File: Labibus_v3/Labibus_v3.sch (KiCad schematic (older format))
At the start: 43 parts, among them J1 Screw_Terminal_01x04, J2 Conn_01x16, J3 Conn_01x06, J4 Conn_01x03, J5 Conn_01x15, J6 Conn_01x12, J7 Conn_01x04 Qwiic JST SH 4-pin, SW1 SW_Push, U1 MIC5205-5.0YM5, U2 MAX485E, U3 ATmega328P-AU, U4 MIC5219-3.3YM5, Y1 Crystal_GND2_Small

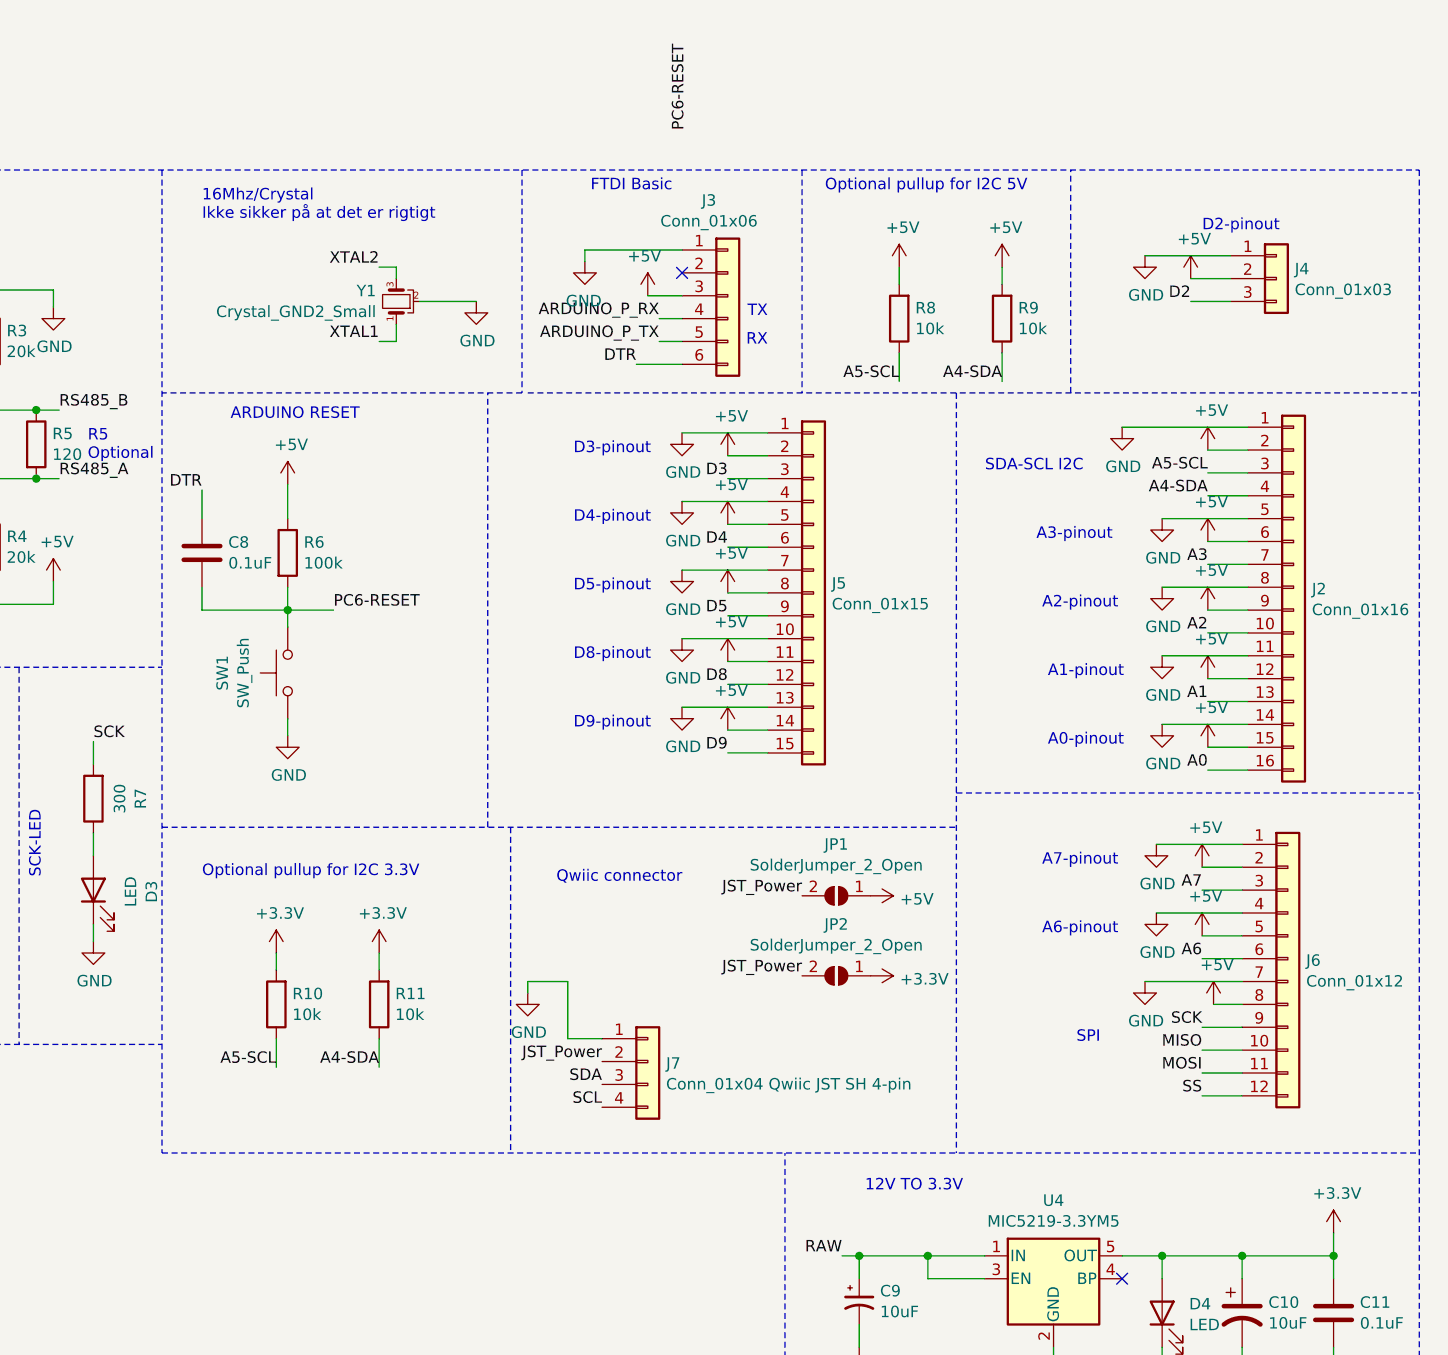
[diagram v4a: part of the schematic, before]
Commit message: update with: 3.3V and 5V select JST connector
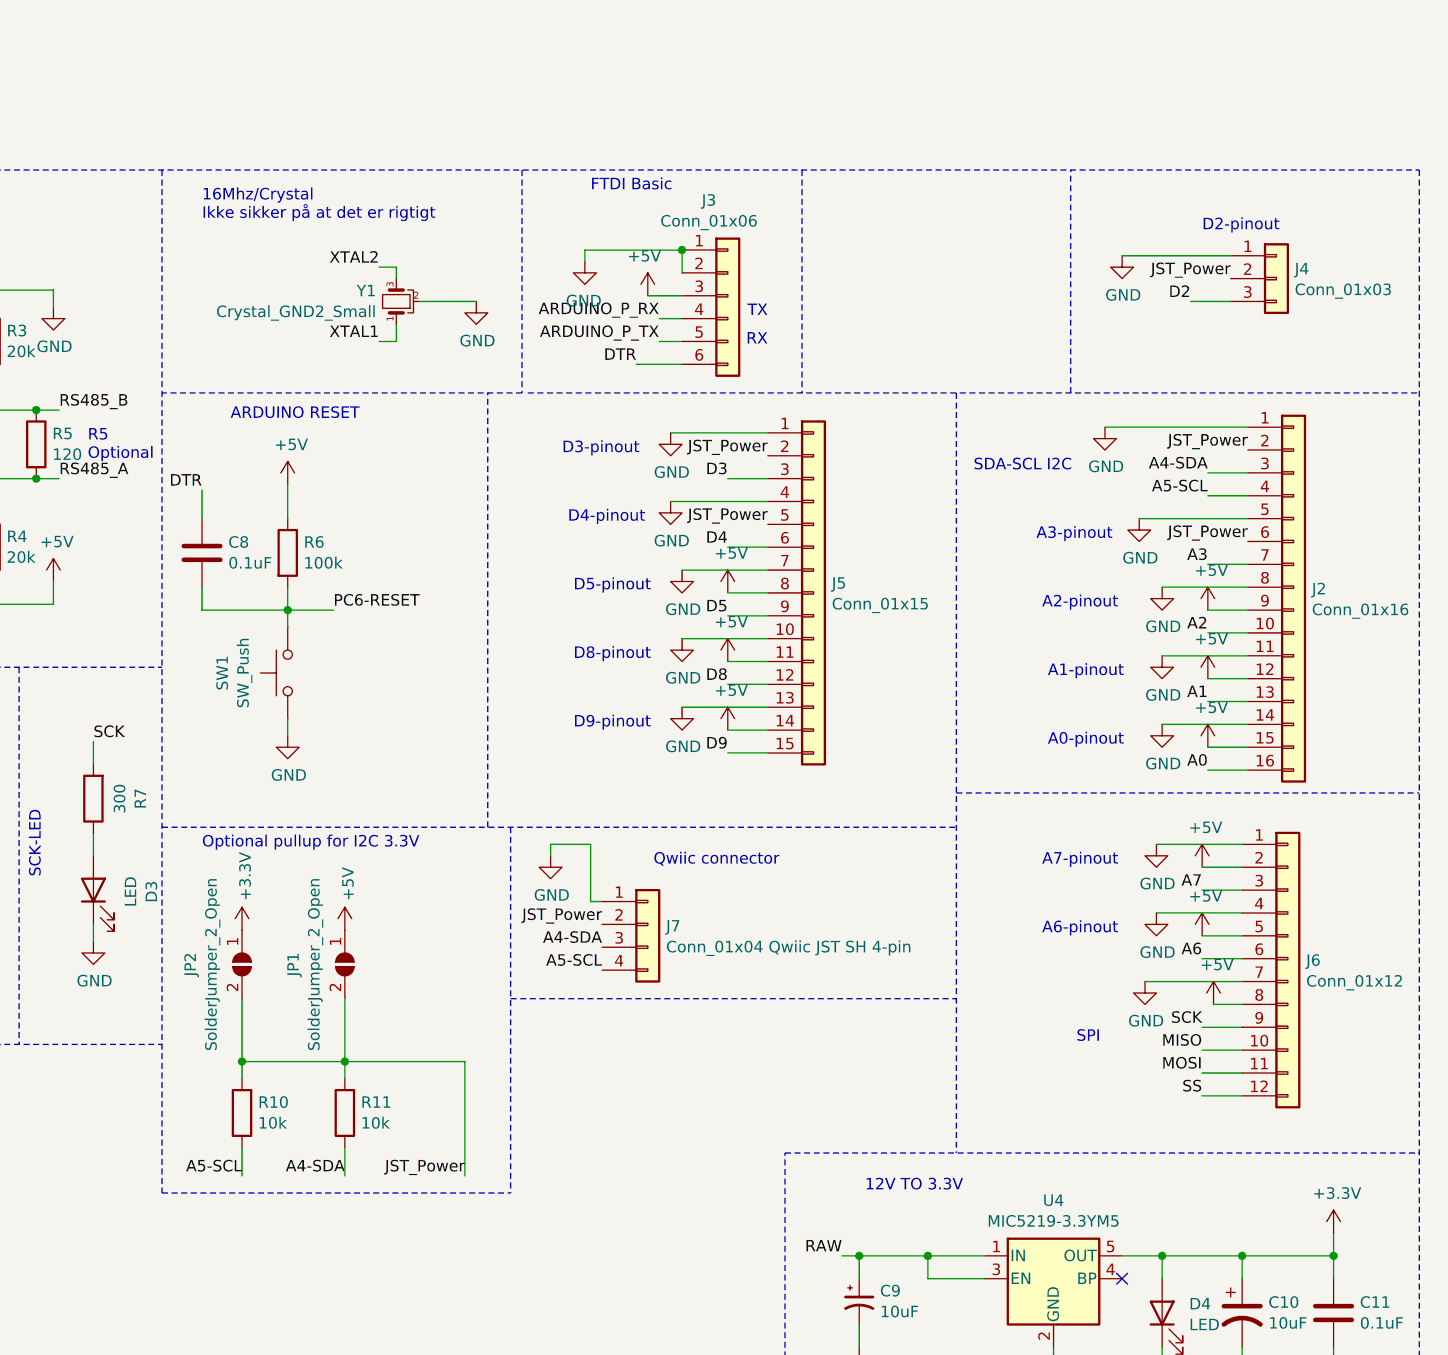
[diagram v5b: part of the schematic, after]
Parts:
- removed R8, R9: 10k, Resistor_SMD:R_0603_1608Metric_Pad0.98x0.95mm_HandSolder, symbol Device:R
- J7: footprint Connector_PinSocket_1.00mm:PinSocket_1x04_P1.00mm_Vertical_SMD_Pin1Left -> Connector_JST:JST_SH_BM04B-SRSS-TB_1x04-1MP_P1.00mm_Vertical
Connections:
- net SCL is gone; now on net A5-SCL: J7.4 (Pin_4)
- net SDA is gone; now on net A4-SDA: J7.3 (Pin_3)
- net +3V3: no longer R10.2, R11.2
- net +5V: no longer J2.2 (Pin_2), J2.6 (Pin_6), J4.2 (Pin_2), J5.2 (Pin_2), J5.5 (Pin_5)
- net A4-SDA: now also J2.3 (Pin_3); no longer J2.4 (Pin_4)
- net A5-SCL: now also J2.4 (Pin_4); no longer J2.3 (Pin_3)
- net GND: now also J3.2 (Pin_2)
- net JST_Power: now also J2.2 (Pin_2), J2.6 (Pin_6), J4.2 (Pin_2), J5.2 (Pin_2), J5.5 (Pin_5), R10.2, R11.2
- no-connect marks 3 -> 2
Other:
- note removed: "Optional pullup for I2C 5V"
- moved on the sheet: J7, JP1, JP2, R10, R11
